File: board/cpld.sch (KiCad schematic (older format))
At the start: 10 parts, among them U19 JIGL, U20 SPI-65B

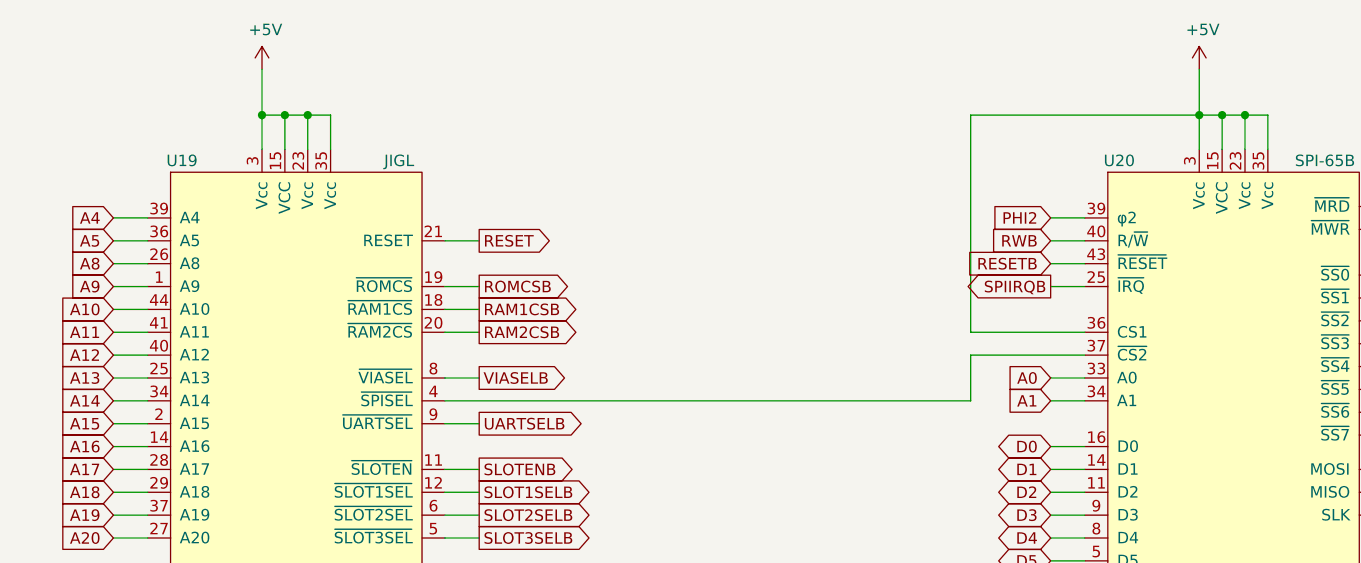
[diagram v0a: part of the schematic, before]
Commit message: RC1 of schematic and initial board layout
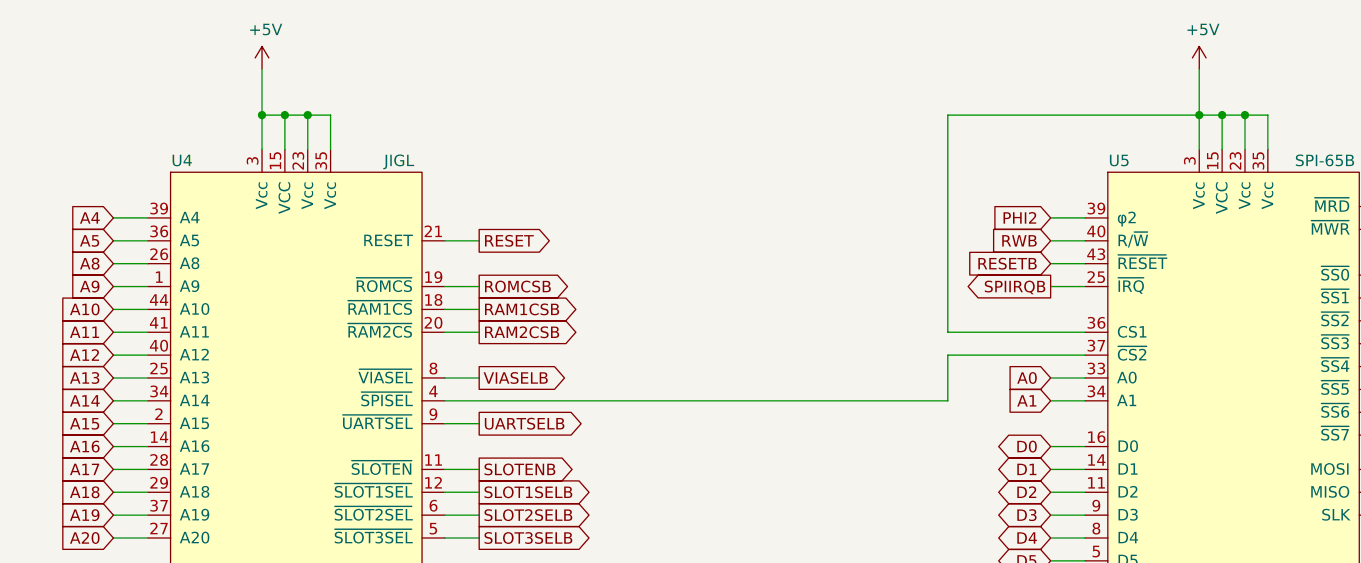
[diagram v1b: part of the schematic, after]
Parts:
- C10: renamed from C44; value 1u -> 0.1u; footprint (none) -> Capacitor_THT:C_Rect_L4.6mm_W2.0mm_P2.50mm_MKS02_FKP02
- C11: renamed from C45; value 1u -> 0.1u; footprint (none) -> Capacitor_THT:C_Rect_L4.6mm_W2.0mm_P2.50mm_MKS02_FKP02
- C4: renamed from C38; value 1u -> 0.1u; footprint (none) -> Capacitor_THT:C_Rect_L4.6mm_W2.0mm_P2.50mm_MKS02_FKP02
- C5: renamed from C39; value 1u -> 0.1u; footprint (none) -> Capacitor_THT:C_Rect_L4.6mm_W2.0mm_P2.50mm_MKS02_FKP02
- C6: renamed from C40; value 1u -> 0.1u; footprint (none) -> Capacitor_THT:C_Rect_L4.6mm_W2.0mm_P2.50mm_MKS02_FKP02
- C7: renamed from C41; value 1u -> 0.1u; footprint (none) -> Capacitor_THT:C_Rect_L4.6mm_W2.0mm_P2.50mm_MKS02_FKP02
- C8: renamed from C42; value 1u -> 0.1u; footprint (none) -> Capacitor_THT:C_Rect_L4.6mm_W2.0mm_P2.50mm_MKS02_FKP02
- C9: renamed from C43; value 1u -> 0.1u; footprint (none) -> Capacitor_THT:C_Rect_L4.6mm_W2.0mm_P2.50mm_MKS02_FKP02
- U4: renamed from U19; footprint (none) -> Package_LCC:PLCC-44_THT-Socket
- U5: renamed from U20; footprint (none) -> Package_LCC:PLCC-44_THT-Socket
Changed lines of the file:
@@
 EELAYER 30 0
 EELAYER END
-$Descr A4 11693 8268
+$Descr USLetter 11000 8500
 encoding utf-8
-Sheet 8 8
+Sheet 3 7
 Title "JRC-1 CPLD Logic"
 Date "2021-12-08"
@@
 P 3550 5350
 AR Path="/60EE1618/62269CB7" Ref="#PWR?"  Part="1"
-AR Path="/6224E7FB/62269CB7" Ref="#PWR096"  Part="1"
-F 0 "#PWR096" H 3550 5100 50  0001 C CNN
+AR Path="/6224E7FB/62269CB7" Ref="#PWR012"  Part="1"
+F 0 "#PWR012" H 3550 5100 50  0001 C CNN
 F 1 "GND" H 3555 5177 50  0000 C CNN
 F 2 "" H 3550 5350 50  0001 C CNN
@@
 P 3550 2300
 AR Path="/60EE1618/62269CBD" Ref="#PWR?"  Part="1"
-AR Path="/6224E7FB/62269CBD" Ref="#PWR095"  Part="1"
-F 0 "#PWR095" H 3550 2150 50  0001 C CNN
+AR Path="/6224E7FB/62269CBD" Ref="#PWR011"  Part="1"
+F 0 "#PWR011" H 3550 2150 50  0001 C CNN
 F 1 "+5V" H 3565 2473 50  0000 C CNN
 F 2 "" H 3550 2300 50  0001 C CNN
@@
 P 3700 3900
 AR Path="/60EE1618/62269CC3" Ref="U?"  Part="1"
-AR Path="/6224E7FB/62269CC3" Ref="U19"  Part="1"
-F 0 "U19" H 3200 5100 50  0000 C CNN
+AR Path="/6224E7FB/62269CC3" Ref="U4"  Part="1"
+F 0 "U4" H 3200 5100 50  0000 C CNN
 F 1 "JIGL" H 4150 5100 50  0000 C CNN
-F 2 "" H 3700 3900 50  0001 C CNN
+F 2 "Package_LCC:PLCC-44_THT-Socket" H 3700 3900 50  0001 C CNN
 F 3 "" H 3700 3900 50  0001 C CNN
 	1    3700 3900
@@
 	4350 4050 4500 4050
 $Comp
-L jrc-1:SPI-65B U20
+L jrc-1:SPI-65B U5
 U 1 1 62947BB2
 P 7800 3900
-F 0 "U20" H 7300 5100 50  0000 C CNN
+F 0 "U5" H 7300 5100 50  0000 C CNN
 F 1 "SPI-65B" H 8200 5100 50  0000 C CNN
-F 2 "" H 6000 4300 50  0001 C CNN
+F 2 "Package_LCC:PLCC-44_THT-Socket" H 6000 4300 50  0001 C CNN
 F 3 "" H 6000 4300 50  0001 C CNN
 	1    7800 3900
@@
 P 7650 2300
 AR Path="/60EE1618/6294A95C" Ref="#PWR?"  Part="1"
-AR Path="/6224E7FB/6294A95C" Ref="#PWR097"  Part="1"
-F 0 "#PWR097" H 7650 2150 50  0001 C CNN
+AR Path="/6224E7FB/6294A95C" Ref="#PWR013"  Part="1"
+F 0 "#PWR013" H 7650 2150 50  0001 C CNN
 F 1 "+5V" H 7665 2473 50  0000 C CNN
 F 2 "" H 7650 2300 50  0001 C CNN
@@
 A0
 Wire Wire Line
-	7650 2500 6650 2500
-Wire Wire Line
-	6650 2500 6650 3450
-Wire Wire Line
-	6650 3450 7150 3450
-Wire Wire Line
-	6650 3750 6650 3550
-Wire Wire Line
-	6650 3550 7150 3550
-Wire Wire Line
-	4350 3750 6650 3750
+	7650 2500 6550 2500
+Wire Wire Line
+	6550 2500 6550 3450
+Wire Wire Line
+	6550 3450 7150 3450
+Wire Wire Line
+	6550 3750 6550 3550
+Wire Wire Line
+	6550 3550 7150 3550
+Wire Wire Line
+	4350 3750 6550 3750
 Wire Wire Line
 	7000 2950 7150 2950
@@
 P 7650 5350
 AR Path="/60EE1618/629825A1" Ref="#PWR?"  Part="1"
-AR Path="/6224E7FB/629825A1" Ref="#PWR098"  Part="1"
-F 0 "#PWR098" H 7650 5100 50  0001 C CNN
+AR Path="/6224E7FB/629825A1" Ref="#PWR014"  Part="1"
+F 0 "#PWR014" H 7650 5100 50  0001 C CNN
 F 1 "GND" H 7655 5177 50  0000 C CNN
 F 2 "" H 7650 5350 50  0001 C CNN
@@
 P 2150 7500
 AR Path="/60EE1618/635CDFA5" Ref="#PWR?"  Part="1"
-AR Path="/6224E7FB/635CDFA5" Ref="#PWR094"  Part="1"
-F 0 "#PWR094" H 2150 7250 50  0001 C CNN
+AR Path="/6224E7FB/635CDFA5" Ref="#PWR010"  Part="1"
+F 0 "#PWR010" H 2150 7250 50  0001 C CNN
 F 1 "GND" H 2155 7327 50  0000 C CNN
 F 2 "" H 2150 7500 50  0001 C CNN
@@
 P 750 7200
 AR Path="/60EE1618/635CDFAB" Ref="C?"  Part="1"
-AR Path="/6224E7FB/635CDFAB" Ref="C38"  Part="1"
-F 0 "C38" H 842 7246 50  0001 L CNN
-F 1 "1u" H 842 7200 50  0001 L CNN
-F 2 "" H 750 7200 50  0001 C CNN
+AR Path="/6224E7FB/635CDFAB" Ref="C4"  Part="1"
+F 0 "C4" H 842 7246 50  0001 L CNN
+F 1 "0.1u" H 842 7200 50  0001 L CNN
+F 2 "Capacitor_THT:C_Rect_L4.6mm_W2.0mm_P2.50mm_MKS02_FKP02" H 750 7200 50  0001 C CNN
 F 3 "~" H 750 7200 50  0001 C CNN
 	1    750  7200
@@
 P 750 6900
 AR Path="/60EE1618/635CDFB1" Ref="#PWR?"  Part="1"
-AR Path="/6224E7FB/635CDFB1" Ref="#PWR093"  Part="1"
-F 0 "#PWR093" H 750 6750 50  0001 C CNN
+AR Path="/6224E7FB/635CDFB1" Ref="#PWR09"  Part="1"
+F 0 "#PWR09" H 750 6750 50  0001 C CNN
 F 1 "+5V" H 765 7073 50  0000 C CNN
 F 2 "" H 750 6900 50  0001 C CNN
@@
 P 950 7200
 AR Path="/60EE1618/635CDFB7" Ref="C?"  Part="1"
-AR Path="/6224E7FB/635CDFB7" Ref="C39"  Part="1"
-F 0 "C39" H 1042 7246 50  0001 L CNN
-F 1 "1u" H 1042 7200 50  0001 L CNN
-F 2 "" H 950 7200 50  0001 C CNN
+AR Path="/6224E7FB/635CDFB7" Ref="C5"  Part="1"
+F 0 "C5" H 1042 7246 50  0001 L CNN
+F 1 "0.1u" H 1042 7200 50  0001 L CNN
+F 2 "Capacitor_THT:C_Rect_L4.6mm_W2.0mm_P2.50mm_MKS02_FKP02" H 950 7200 50  0001 C CNN
 F 3 "~" H 950 7200 50  0001 C CNN
 	1    950  7200
@@
 P 1150 7200
 AR Path="/60EE1618/635CDFBD" Ref="C?"  Part="1"
-AR Path="/6224E7FB/635CDFBD" Ref="C40"  Part="1"
-F 0 "C40" H 1242 7246 50  0001 L CNN
-F 1 "1u" H 1242 7200 50  0001 L CNN
-F 2 "" H 1150 7200 50  0001 C CNN
+AR Path="/6224E7FB/635CDFBD" Ref="C6"  Part="1"
+F 0 "C6" H 1242 7246 50  0001 L CNN
+F 1 "0.1u" H 1242 7200 50  0001 L CNN
+F 2 "Capacitor_THT:C_Rect_L4.6mm_W2.0mm_P2.50mm_MKS02_FKP02" H 1150 7200 50  0001 C CNN
 F 3 "~" H 1150 7200 50  0001 C CNN
 	1    1150 7200
@@
 P 1350 7200
 AR Path="/60EE1618/635CDFC3" Ref="C?"  Part="1"
-AR Path="/6224E7FB/635CDFC3" Ref="C41"  Part="1"
-F 0 "C41" H 1442 7246 50  0001 L CNN
-F 1 "1u" H 1442 7200 50  0001 L CNN
-F 2 "" H 1350 7200 50  0001 C CNN
+AR Path="/6224E7FB/635CDFC3" Ref="C7"  Part="1"
+F 0 "C7" H 1442 7246 50  0001 L CNN
+F 1 "0.1u" H 1442 7200 50  0001 L CNN
+F 2 "Capacitor_THT:C_Rect_L4.6mm_W2.0mm_P2.50mm_MKS02_FKP02" H 1350 7200 50  0001 C CNN
 F 3 "~" H 1350 7200 50  0001 C CNN
 	1    1350 7200
@@
 P 1550 7200
 AR Path="/60EE1618/635CDFC9" Ref="C?"  Part="1"
-AR Path="/6224E7FB/635CDFC9" Ref="C42"  Part="1"
-F 0 "C42" H 1642 7246 50  0001 L CNN
-F 1 "1u" H 1642 7200 50  0001 L CNN
-F 2 "" H 1550 7200 50  0001 C CNN
+AR Path="/6224E7FB/635CDFC9" Ref="C8"  Part="1"
+F 0 "C8" H 1642 7246 50  0001 L CNN
+F 1 "0.1u" H 1642 7200 50  0001 L CNN
+F 2 "Capacitor_THT:C_Rect_L4.6mm_W2.0mm_P2.50mm_MKS02_FKP02" H 1550 7200 50  0001 C CNN
 F 3 "~" H 1550 7200 50  0001 C CNN
 	1    1550 7200
@@
 P 1750 7200
 AR Path="/60EE1618/635CDFEB" Ref="C?"  Part="1"
-AR Path="/6224E7FB/635CDFEB" Ref="C43"  Part="1"
-F 0 "C43" H 1842 7246 50  0001 L CNN
-F 1 "1u" H 1842 7200 50  0001 L CNN
-F 2 "" H 1750 7200 50  0001 C CNN
+AR Path="/6224E7FB/635CDFEB" Ref="C9"  Part="1"
+F 0 "C9" H 1842 7246 50  0001 L CNN
+F 1 "0.1u" H 1842 7200 50  0001 L CNN
+F 2 "Capacitor_THT:C_Rect_L4.6mm_W2.0mm_P2.50mm_MKS02_FKP02" H 1750 7200 50  0001 C CNN
 F 3 "~" H 1750 7200 50  0001 C CNN
 	1    1750 7200
@@
 P 1950 7200
 AR Path="/60EE1618/635CDFF6" Ref="C?"  Part="1"
-AR Path="/6224E7FB/635CDFF6" Ref="C44"  Part="1"
-F 0 "C44" H 2042 7246 50  0001 L CNN
-F 1 "1u" H 2042 7200 50  0001 L CNN
-F 2 "" H 1950 7200 50  0001 C CNN
+AR Path="/6224E7FB/635CDFF6" Ref="C10"  Part="1"
+F 0 "C10" H 2042 7246 50  0001 L CNN
+F 1 "0.1u" H 2042 7200 50  0001 L CNN
+F 2 "Capacitor_THT:C_Rect_L4.6mm_W2.0mm_P2.50mm_MKS02_FKP02" H 1950 7200 50  0001 C CNN
 F 3 "~" H 1950 7200 50  0001 C CNN
 	1    1950 7200
@@
 P 2150 7200
 AR Path="/60EE1618/635D31AA" Ref="C?"  Part="1"
-AR Path="/6224E7FB/635D31AA" Ref="C45"  Part="1"
-F 0 "C45" H 2242 7246 50  0001 L CNN
-F 1 "1u" H 2242 7200 50  0001 L CNN
-F 2 "" H 2150 7200 50  0001 C CNN
+AR Path="/6224E7FB/635D31AA" Ref="C11"  Part="1"
+F 0 "C11" H 2242 7246 50  0001 L CNN
+F 1 "0.1u" H 2242 7200 50  0001 L CNN
+F 2 "Capacitor_THT:C_Rect_L4.6mm_W2.0mm_P2.50mm_MKS02_FKP02" H 2150 7200 50  0001 C CNN
 F 3 "~" H 2150 7200 50  0001 C CNN
 	1    2150 7200

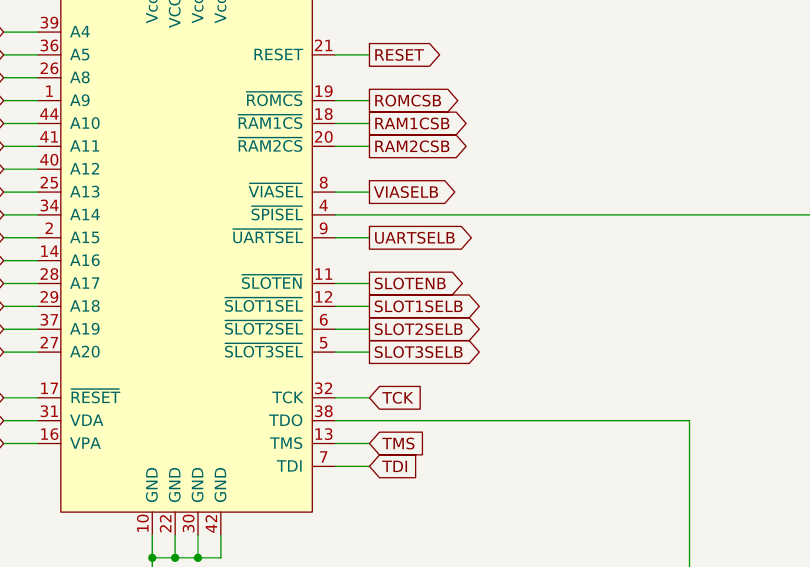
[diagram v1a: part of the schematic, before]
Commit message: RC1 of schematic and initial board layout
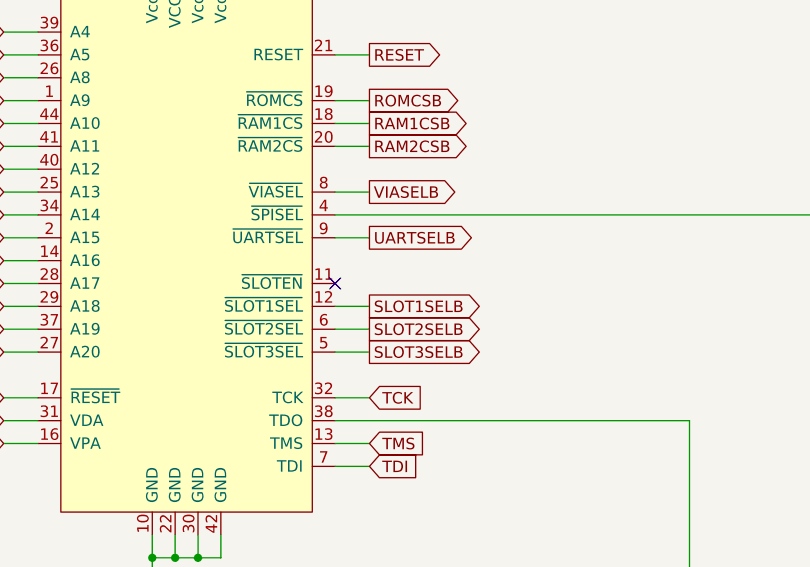
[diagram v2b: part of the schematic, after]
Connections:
- net SLOTENB: no longer names the net of U4.11 (~SLOTEN)
- no-connect marks 1 -> 2
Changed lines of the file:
@@
 Wire Wire Line
 	4350 4850 4500 4850
-Text GLabel 4500 4050 2    50   Output ~ 0
-SLOTENB
-Wire Wire Line
-	4350 4050 4500 4050
 $Comp
 L jrc-1:SPI-65B U5
@@
 Text GLabel 4500 3050 2    50   Output ~ 0
 RESET
+NoConn ~ 4350 4050
 $EndSCHEMATC
